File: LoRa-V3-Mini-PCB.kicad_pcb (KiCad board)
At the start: 2 copper layers, 52 x 18 mm, 24 parts, among them Q1 SI2367DS-T1-GE3, SW1 434331045822, SW2 434331045816, U1 114993121, U2 BR24G1MFVT, U3 SHT40, U4 TSL25911

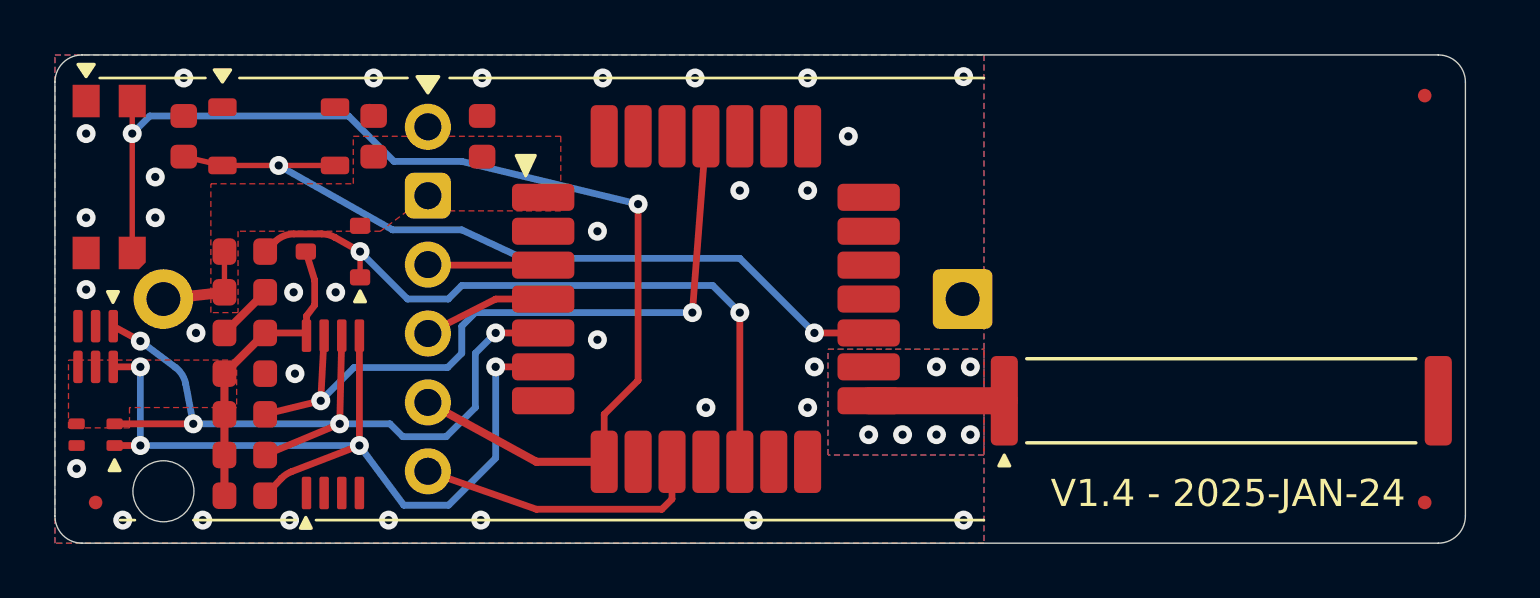
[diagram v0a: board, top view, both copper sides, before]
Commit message: change caps to 0805
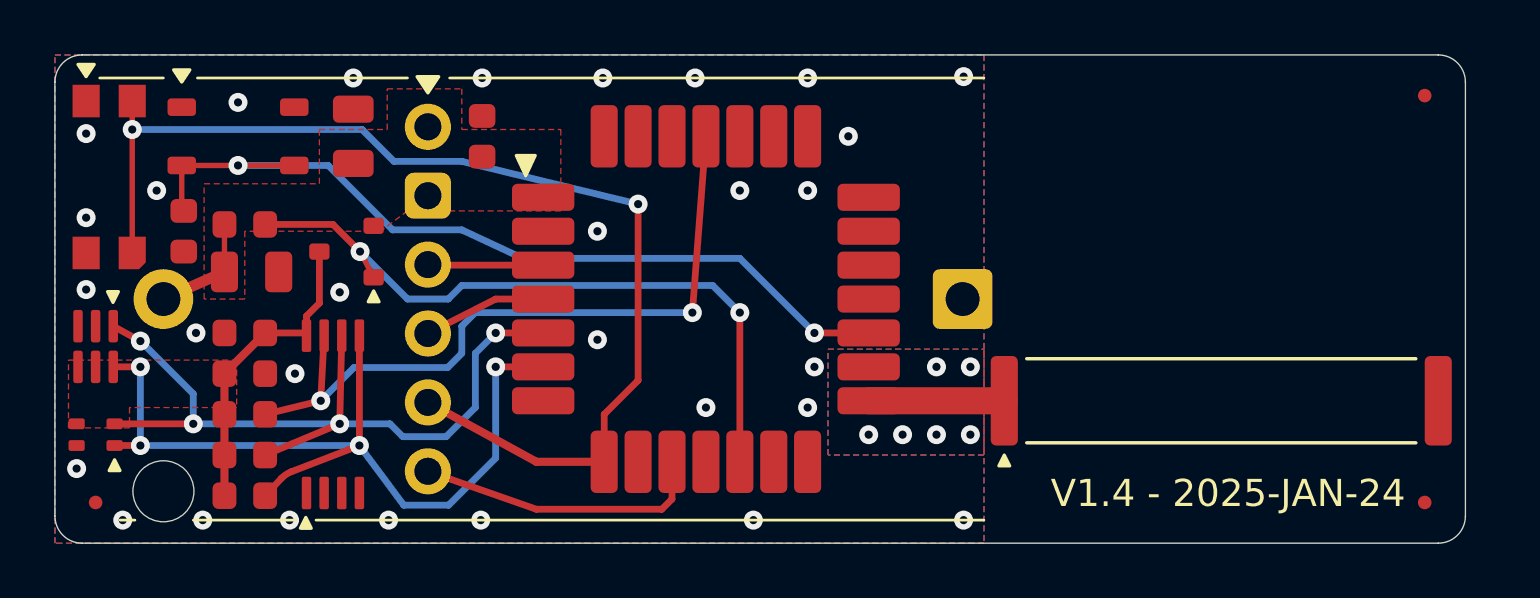
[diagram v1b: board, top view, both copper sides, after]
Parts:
- C10, C11: footprint 1projectLibrary:C_0603_nominal -> 1GlobalFootprintsLibrary:C_0805
- moved C5 3.50 mm to (133.7, 101.0), turned to -90 degrees
- moved SW2 1.50 mm to (135.7, 97.5)
- moved R4 1.00 mm to (135.9, 100.8)
- moved C10 0.79 mm to (136.2, 102.5)
- moved C11 0.75 mm to (139.9, 97.5)
- moved Q1 0.50 mm to (139.7, 101.8)
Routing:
- net GND: track 2.53 -> 0.25 mm, vias 38 -> 36
- net Net-(U1-RST): track 29.4 -> 31.5 mm

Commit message: fix BOM
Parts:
- ANT1: value ANT-868-CHP-T -> Chip Antenna
- BH1: value 108 -> Battery Holder
- C1, C2, C3, C5: value CGA3E2X7R1E104K080AA -> 100nF
- C10, C11: value C1608X7S1A475K080AC -> 4.7uF; footprint 1GlobalFootprintsLibrary:C_0805 -> 1projectLibrary:C_0805
- Q1: value SI2367DS-T1-GE3 -> NA
- R1, R2, R3: value CR0603-FX-4701ELF -> 4K7
- R4: value CR0603-FX-1004ELF -> 330K
- SW1: value 434331045822 -> Application Button
- SW2: value 434331045816 -> MCU Reset
- U1: value 114993121 -> Lora-E5
